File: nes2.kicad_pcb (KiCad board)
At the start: 4 copper layers, 100 x 122.7 mm, 79 parts, among them CN2 NES Card Edge, J1 NES 5v TP, J2 NES 3v3 TP, J3 NES PWR, J4 VGA, J5 AUDIO_EXP, U1 74ALVC164245, U2 74ALVC164245, U3 74ALVC164245, U4 74ALVC164245, U5 IS61C5128AL-10TLI, U6 IS61C5128AL-10TLI, U7 LM3671-3.3, U8 LM3671-1.2

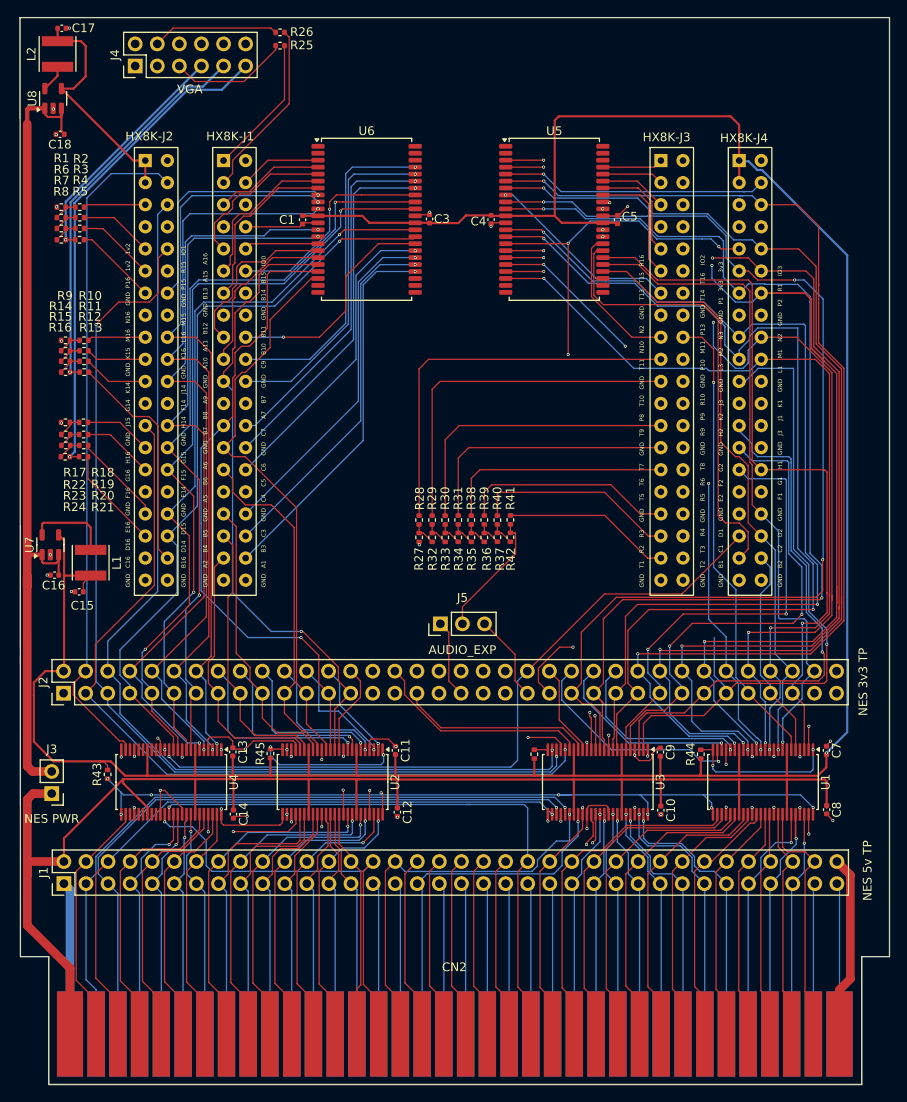
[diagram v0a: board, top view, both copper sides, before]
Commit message: Update trace spacing and copper fills.
Signed-off-by: Chris Frantz <frantzcj@gmail.com>
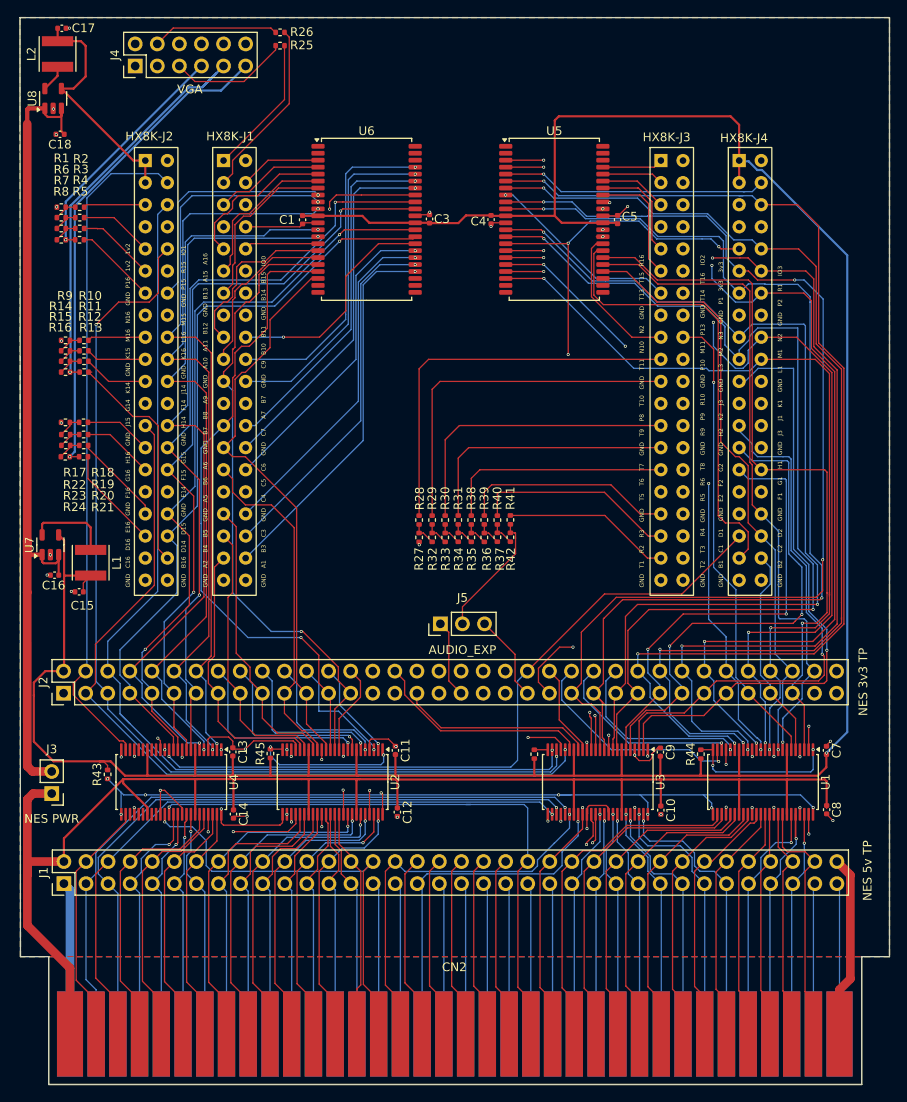
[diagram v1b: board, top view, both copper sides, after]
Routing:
- net CPU_D7: track 111.2 -> 104.9 mm
- net PPU_RD#: track 103.5 -> 106.7 mm
- net CPU_A6: track 109.5 -> 106.9 mm
- net /Expansion/GRN: track 44.8 -> 46.7 mm
- net CIC_PK: track 116.4 -> 118.0 mm
- net NES_PPU_RD#: track 46.5 -> 45.6 mm
- net NES_PPU_A13: track 33.6 -> 33.0 mm
- added copper zone on B.Cu, net GND
- added copper zone on F.Cu, net GND

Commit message: Re-do the board layout
Signed-off-by: Chris Frantz <frantzcj@gmail.com>
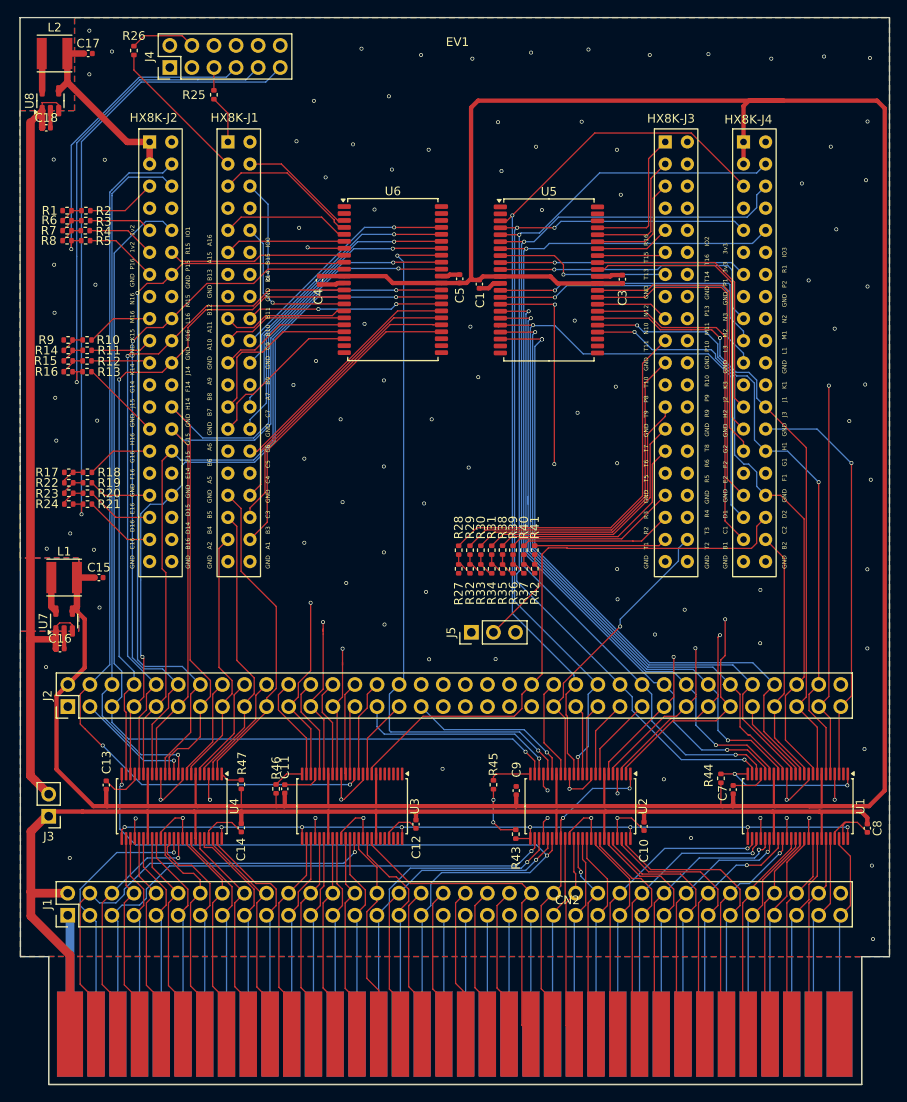
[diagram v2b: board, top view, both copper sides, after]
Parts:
- added R47: 10k, Resistor_SMD:R_0402_1005Metric, F.Cu at (139.0, 119.5)
- U7, U8: footprint Package_TO_SOT_SMD:SOT-23-5 -> Package_TO_SOT_SMD:TSOT-23-5
- moved R43 47.4 mm to (170.6, 125.2)
- moved R46 30.0 mm to (143.0, 120.0)
- moved U2 28.6 mm to (178.0, 122.0)
- moved U3 28.4 mm to (151.8, 122.0)
- moved R45 25.9 mm to (168.0, 119.5)
- moved C3 23.2 mm to (182.8, 61.4)
- moved C1 21.6 mm to (166.4, 62.0)
- moved C4 20.9 mm to (148.0, 61.5)
- moved C5 19.4 mm to (164.1, 61.3)
- moved C9 17.2 mm to (170.6, 120.2)
- moved R26 16.9 mm to (126.7, 35.1), turned to 90 degrees
- moved C13 15.0 mm to (123.5, 119.6)
- moved C11 13.5 mm to (144.0, 120.0)
- moved C7 11.6 mm to (195.6, 120.1)
- moved R25 9.48 mm to (135.8, 40.2), turned to 90 degrees
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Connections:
- EV1 pad J2P14: /Expansion/VGA_B0 -> /Expansion/VGA_G3
- EV1 pad J2P15: /Expansion/VGA_B1 -> /Expansion/VGA_B0
- EV1 pad J2P17: /Expansion/VGA_B2 -> /Expansion/VGA_B1
- EV1 pad J2P18: /Expansion/VGA_B3 -> /Expansion/VGA_B2
- EV1 pad J2P19: CONV -> /Expansion/VGA_B3
- EV1 pad J2P26: unconnected-(EV1A-L16-PadJ2P26) -> ECHR_CE#
- EV1 pad J2P27: ECHR_CE# -> PPU_D0
- EV1 pad J2P29: PPU_D0 -> PPU_D1
- EV1 pad J2P30: PPU_D1 -> PPU_D2
- EV1 pad J2P31: PPU_D2 -> PPU_D3
- EV1 pad J2P33: PPU_D3 -> PPU_D7
- EV1 pad J2P34: PPU_D7 -> PPU_D6
- EV1 pad J2P35: PPU_D6 -> PPU_D5
- EV1 pad J2P37: PPU_D5 -> PPU_D4
- EV1 pad J2P38: PPU_D4 -> unconnected-(EV1A-D14-PadJ2P38)
- EV1 pad J2P39: /Expansion/VGA_G3 -> CONV
- EV1 pad J3P20: unconnected-(EV1C-GND-PadJ3P20) -> GND
- EV1 pad J3P23: /Expansion/GPIO1 -> unconnected-(EV1C-T14-PadJ3P23)
- EV1 pad J3P25: /Expansion/GPIO2 -> unconnected-(EV1C-P13-PadJ3P25)
- EV1 pad J3P26: /Expansion/GPIO3 -> unconnected-(EV1C-M11-PadJ3P26)
- EV1 pad J3P27: ROMSEL# -> unconnected-(EV1C-P10-PadJ3P27)
- EV1 pad J3P30: /Expansion/GPIO4 -> unconnected-(EV1C-P9-PadJ3P30)
- EV1 pad J3P32: unconnected-(EV1C-GND-PadJ3P32) -> GND
- EV1 pad J3P33: /Expansion/GPIO6 -> unconnected-(EV1C-T8-PadJ3P33)
- EV1 pad J3P34: /Expansion/GPIO7 -> unconnected-(EV1C-R6-PadJ3P34)
- EV1 pad J3P35: /Expansion/GPIO8 -> unconnected-(EV1C-R5-PadJ3P35)
- EV1 pad J3P37: /Expansion/GPIO9 -> unconnected-(EV1C-R4-PadJ3P37)
- EV1 pad J3P38: /Expansion/GPIO10 -> unconnected-(EV1C-T3-PadJ3P38)
- EV1 pad J3P39: /Expansion/GPIO11 -> ROMSEL#
- EV1 pad J4P10: CPU_D3 -> CPU_D2
- EV1 pad J4P11: CPU_D7 -> CPU_D3
- EV1 pad J4P13: CPU_D6 -> CPU_D7
- EV1 pad J4P14: CPU_D5 -> CPU_D6
- EV1 pad J4P15: CPU_D4 -> CPU_D5
- EV1 pad J4P17: CPU_A7 -> CPU_D4
- EV1 pad J4P18: IRQ# -> CPU_A7
- EV1 pad J4P33: unconnected-(EV1D-H1-PadJ4P33) -> CPU_A12
- EV1 pad J4P35: CPU_A12 -> CPU_A11
- EV1 pad J4P37: CPU_A11 -> CPU_A10
- EV1 pad J4P38: CPU_A10 -> IRQ#
- EV1 pad J4P4: CPU_A1 -> GND
- EV1 pad J4P5: CPU_RW# -> CPU_A1
- EV1 pad J4P6: CPU_D0 -> CPU_RW#
- EV1 pad J4P7: CPU_D1 -> CPU_D0
- EV1 pad J4P9: CPU_D2 -> CPU_D1
- R45 pad 2: Net-(U2-1DIR) -> Net-(U2-2DIR)
- U1 pad 11: CPU_A9 -> CPU_A13
- U1 pad 12: CPU_A8 -> CPU_A9
- U1 pad 13: CPU_A7 -> CPU_A14
- U1 pad 14: CPU_A6 -> CPU_A8
- U1 pad 16: CPU_A5 -> CPU_A7
- U1 pad 17: CPU_A4 -> CPU_A6
- U1 pad 19: CPU_A3 -> CPU_A5
- U1 pad 2: ROMSEL# -> unconnected-(U1-1B0-Pad2)
- U1 pad 20: CPU_A2 -> CPU_A4
- U1 pad 22: CPU_A1 -> CPU_A3
- U1 pad 23: CPU_A0 -> CPU_A2
- U1 pad 26: NES_CPU_A0 -> NES_CPU_A2
- U1 pad 27: NES_CPU_A1 -> NES_CPU_A3
- U1 pad 29: NES_CPU_A2 -> NES_CPU_A4
- U1 pad 3: CPU_A12 -> CLK
- U1 pad 30: NES_CPU_A3 -> NES_CPU_A5
- U1 pad 32: NES_CPU_A4 -> NES_CPU_A6
- U1 pad 33: NES_CPU_A5 -> NES_CPU_A7
- U1 pad 35: NES_CPU_A6 -> NES_CPU_A8
- U1 pad 36: NES_CPU_A7 -> NES_CPU_A14
- U1 pad 37: NES_CPU_A8 -> NES_CPU_A9
- U1 pad 38: NES_CPU_A9 -> NES_CPU_A13
- U1 pad 41: NES_CPU_A11 -> NES_CPU_A12
- U1 pad 43: NES_CPU_A14 -> NES_CPU_A11
- U1 pad 44: NES_CPU_A13 -> NES_M2
- U1 pad 46: NES_CPU_A12 -> NES_CLK
- U1 pad 47: NES_ROMSEL# -> GND
- U1 pad 5: CPU_A13 -> M2
- U1 pad 6: CPU_A14 -> CPU_A11
- U1 pad 8: CPU_A11 -> CPU_A12
- U2 pad 1: Net-(U2-1DIR) -> NES_CPU_RW#
- U2 pad 11: PPU_A6 -> CPU_D1
- U2 pad 12: PPU_A7 -> CPU_D0
- U2 pad 13: PPU_A8 -> CPU_A1
- U2 pad 14: PPU_A9 -> CPU_A0
- U2 pad 16: PPU_A10 -> ROMSEL#
- U2 pad 17: PPU_A11 -> CPU_RW#
- U2 pad 19: PPU_A12 -> PPU_WR#
- U2 pad 2: PPU_A5 -> CPU_D7
- U2 pad 20: PPU_A13 -> PPU_RD#
- U2 pad 22: CIRAM_CE# -> PPU_A13#
- U2 pad 23: PPU_A13# -> CIC_RST
- U2 pad 24: Net-(U2-1DIR) -> Net-(U2-2DIR)
- U2 pad 26: NES_PPU_A13# -> NES_CIC_RST
- U2 pad 27: NES_CIRAM_CE# -> NES_PPU_A13#
- U2 pad 29: NES_PPU_A13 -> NES_PPU_RD#
- U2 pad 3: PPU_A4 -> CPU_D6
- U2 pad 30: NES_PPU_A12 -> NES_PPU_WR#
- U2 pad 32: NES_PPU_A11 -> NES_CPU_RW#
- U2 pad 33: NES_PPU_A10 -> NES_ROMSEL#
- U2 pad 35: NES_PPU_A9 -> NES_CPU_A0
- U2 pad 36: NES_PPU_A8 -> NES_CPU_A1
- U2 pad 37: NES_PPU_A7 -> NES_CPU_D0
- U2 pad 38: NES_PPU_A6 -> NES_CPU_D1
- U2 pad 40: NES_PPU_A0 -> NES_CPU_D2
- U2 pad 41: NES_PPU_A1 -> NES_CPU_D3
- U2 pad 43: NES_PPU_A2 -> NES_CPU_D4
- U2 pad 44: NES_PPU_A3 -> NES_CPU_D5
- U2 pad 46: NES_PPU_A4 -> NES_CPU_D6
- U2 pad 47: NES_PPU_A5 -> NES_CPU_D7
- U2 pad 5: PPU_A3 -> CPU_D5
- U2 pad 6: PPU_A2 -> CPU_D4
- U2 pad 8: PPU_A1 -> CPU_D3
- U2 pad 9: PPU_A0 -> CPU_D2
- U3 pad 1: NES_CPU_RW# -> GND
- U3 pad 11: CPU_D1 -> CIRAM_A10
- U3 pad 12: CPU_D0 -> CIC_MB
- U3 pad 13: CLK -> PPU_A7
- U3 pad 14: M2 -> PPU_A6
- U3 pad 16: CPU_RW# -> PPU_A8
- U3 pad 17: PPU_WR# -> PPU_A5
- U3 pad 19: PPU_RD# -> PPU_A9
- U3 pad 2: CPU_D7 -> GND
- U3 pad 20: CIC_CLK -> PPU_A4
- U3 pad 22: CIC_RST -> PPU_A10
- U3 pad 23: CIC_PK -> PPU_A3
- U3 pad 26: NES_CIC_PK -> NES_PPU_A3
- U3 pad 27: NES_CIC_RST -> NES_PPU_A10
- U3 pad 29: NES_CIC_CLK -> NES_PPU_A4
- U3 pad 3: CPU_D6 -> GND
- U3 pad 30: NES_PPU_RD# -> NES_PPU_A9
- U3 pad 32: NES_PPU_WR# -> NES_PPU_A5
- U3 pad 33: NES_CPU_RW# -> NES_PPU_A8
- U3 pad 35: NES_M2 -> NES_PPU_A6
- U3 pad 36: NES_CLK -> NES_PPU_A7
- U3 pad 37: NES_CPU_D0 -> NES_CIC_MB
- U3 pad 38: NES_CPU_D1 -> NES_CIRAM_A10
- U3 pad 40: NES_CPU_D2 -> NES_CIRAM_CE#
- U3 pad 41: NES_CPU_D3 -> NES_IRQ#
- U3 pad 43: NES_CPU_D4 -> unconnected-(U3-1A3-Pad43)
- U3 pad 44: NES_CPU_D5 -> unconnected-(U3-1A2-Pad44)
- U3 pad 46: NES_CPU_D6 -> unconnected-(U3-1A1-Pad46)
- U3 pad 47: NES_CPU_D7 -> unconnected-(U3-1A0-Pad47)
- U3 pad 5: CPU_D5 -> GND
- U3 pad 6: CPU_D4 -> GND
- U3 pad 8: CPU_D3 -> IRQ#
- U3 pad 9: CPU_D2 -> CIRAM_CE#
- U4 pad 1: NES_PPU_WR# -> Net-(U4-1DIR)
- U4 pad 11: PPU_D5 -> CIC_PK
- U4 pad 12: PPU_D4 -> CIC_CLK
- U4 pad 13: IRQ# -> PPU_D7
- U4 pad 14: CIRAM_A10 -> PPU_D0
- U4 pad 16: unconnected-(U4-2B2-Pad16) -> PPU_D6
- U4 pad 17: unconnected-(U4-2B3-Pad17) -> PPU_D1
- U4 pad 19: unconnected-(U4-2B4-Pad19) -> PPU_D5
- U4 pad 2: PPU_D0 -> PPU_A11
- U4 pad 20: unconnected-(U4-2B5-Pad20) -> PPU_D2
- U4 pad 22: unconnected-(U4-2B6-Pad22) -> PPU_D4
- U4 pad 23: CIC_MB -> PPU_D3
- U4 pad 24: GND -> NES_PPU_WR#
- U4 pad 26: NES_CIC_MB -> NES_PPU_D3
- U4 pad 27: unconnected-(U4-2A6-Pad27) -> NES_PPU_D4
- U4 pad 29: unconnected-(U4-2A5-Pad29) -> NES_PPU_D2
- U4 pad 3: PPU_D1 -> PPU_A2
- U4 pad 30: unconnected-(U4-2A4-Pad30) -> NES_PPU_D5
- U4 pad 32: unconnected-(U4-2A3-Pad32) -> NES_PPU_D1
- U4 pad 33: unconnected-(U4-2A2-Pad33) -> NES_PPU_D6
- U4 pad 35: NES_CIRAM_A10 -> NES_PPU_D0
- U4 pad 36: NES_IRQ# -> NES_PPU_D7
- U4 pad 37: NES_PPU_D4 -> NES_CIC_CLK
- U4 pad 38: NES_PPU_D5 -> NES_CIC_PK
- U4 pad 40: NES_PPU_D6 -> NES_PPU_A0
- U4 pad 41: NES_PPU_D7 -> NES_PPU_A13
- U4 pad 43: NES_PPU_D3 -> NES_PPU_A1
- U4 pad 44: NES_PPU_D2 -> NES_PPU_A12
- U4 pad 46: NES_PPU_D1 -> NES_PPU_A2
- U4 pad 47: NES_PPU_D0 -> NES_PPU_A11
- U4 pad 5: PPU_D2 -> PPU_A12
- U4 pad 6: PPU_D3 -> PPU_A1
- U4 pad 8: PPU_D7 -> PPU_A13
- U4 pad 9: PPU_D6 -> PPU_A0
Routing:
- net ROMSEL#: track 94.3 -> 33.9 mm, vias 2 -> 1
- net 3v3: track 318.8 -> 369.4 mm, vias 1 -> 2
- net NES_CIC_CLK: track 78.9 -> 31.6 mm
- net NES_CIC_PK: track 76.0 -> 29.0 mm
- net CIC_CLK: track 95.1 -> 52.2 mm
- net CIC_PK: track 118.0 -> 81.4 mm
- net CPU_A7: track 79.5 -> 115.3 mm, vias 4 -> 1
- net NES_IRQ#: track 69.9 -> 38.5 mm, vias 1 -> 0
- net NES_ROMSEL#: track 52.8 -> 23.1 mm, vias 1 -> 0
- net NES_CLK: track 52.4 -> 23.5 mm, vias 1 -> 0
- net CPU_D0: track 121.9 -> 93.1 mm, vias 3 -> 1
- net CIC_MB: track 77.7 -> 106.4 mm, vias 0 -> 2
- net NES_M2: track 49.9 -> 23.3 mm, vias 1 -> 0
- net NES_CIRAM_A10: track 50.4 -> 24.4 mm, vias 1 -> 0
- net NES_CIC_MB: track 28.6 -> 52.7 mm, vias 0 -> 1
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
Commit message: Incorporate review feedback
Signed-off-by: Chris Frantz <frantzcj@gmail.com>
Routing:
- net GND: track 136.4 -> 142.0 mm, vias 110 -> 143
- net NES_PPU_A2: track 26.5 -> 28.7 mm
- net PPU_A4: track 88.9 -> 87.7 mm
- net NES_CLK: track 23.5 -> 24.6 mm
- net NES_PPU_A11: track 26.9 -> 27.8 mm
- net CLK: track 47.8 -> 48.8 mm
- net CPU_A6: track 102.7 -> 101.7 mm
- net NES_PPU_A13: track 25.1 -> 25.9 mm
- net CPU_A9: vias 2 -> 1
